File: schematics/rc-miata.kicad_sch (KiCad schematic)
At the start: 4 parts, among them M1 BLDC_MOTOR, U1 ESP32-C3-DevKitM-1, U3 ESC

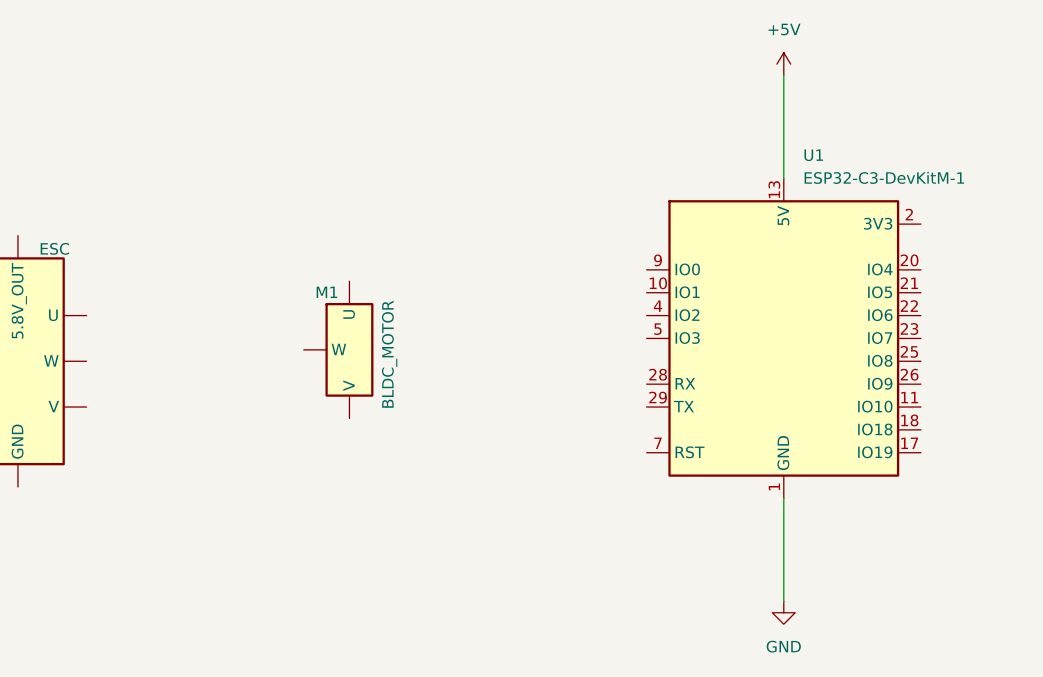
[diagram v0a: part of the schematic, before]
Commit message: Created UBEC symbol. Added UBEC to schematic unwired
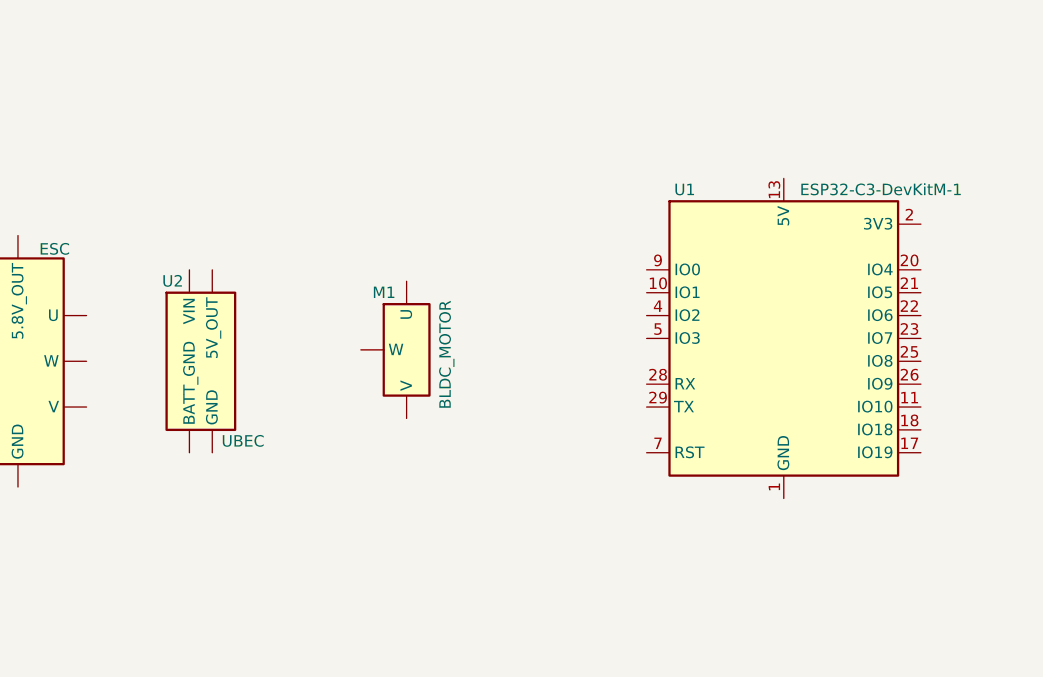
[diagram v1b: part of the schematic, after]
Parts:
- added U2: UBEC, symbol RC Components:UBEC
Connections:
- net +5V: no longer names the net of U1.13 (5V), U1.14 (5V)
- net GND: no longer names the net of U1.1 (GND), U1.12 (GND), U1.15 (GND), U1.16 (GND), U1.19 (GND), U1.24 (GND), U1.27 (GND), U1.30 (GND), U1.6 (GND), U1.8 (GND)
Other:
- moved on the sheet: M1
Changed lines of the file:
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@@
 		(company "TOFFOR AUTOS")
-	)
-	(wire
-		(pts
-			(xy 165.1 66.04) (xy 165.1 77.47)
-		)
-		(stroke
-			(width 0)
-			(type default)
-		)
-	)
-	(wire
-		(pts
-			(xy 165.1 124.46) (xy 165.1 113.03)
-		)
-		(stroke
-			(width 0)
-			(type default)
-		)
 	)
 	(symbol
@@
 		(in_pos_files yes)
 		(dnp no)
-		(fields_autoplaced yes)
 		(property "Reference" "U1"
-			(at 167.2433 74.93 0)
+			(at 152.908 78.74 0)
 			(show_name no)
 			(do_not_autoplace no)
@@
 		)
 		(property "Value" "ESP32-C3-DevKitM-1"
-			(at 167.2433 77.47 0)
+			(at 166.878 78.74 0)
 			(show_name no)
 			(do_not_autoplace no)
@@
 	(symbol
 		(lib_id "RC Components:BLDC_MOTOR")
-		(at 114.3 91.44 0)
+		(at 120.65 91.44 0)
 		(unit 1)
 		(body_style 1)
@@
 		(dnp no)
 		(property "Reference" "M1"
-			(at 113.03 90.17 0)
+			(at 119.38 90.17 0)
 			(show_name no)
 			(do_not_autoplace no)
@@
 		)
 		(property "Value" "BLDC_MOTOR"
-			(at 121.158 103.124 90)
+			(at 127.508 103.124 90)
 			(show_name no)
 			(do_not_autoplace no)
@@
 		)
 		(property "Footprint" ""
-			(at 114.3 91.44 0)
+			(at 120.65 91.44 0)
 			(hide yes)
 			(show_name no)
@@
 		)
 		(property "Datasheet" ""
-			(at 114.3 91.44 0)
+			(at 120.65 91.44 0)
 			(hide yes)
 			(show_name no)
@@
 		)
 		(property "Description" "Brushless DC motor, 3100Kv, Made for 1/10 RC Cars"
-			(at 152.4 98.552 0)
+			(at 158.75 98.552 0)
 			(hide yes)
 			(show_name no)
@@
 	)
 	(symbol
-		(lib_id "power:GND")
-		(at 165.1 124.46 0)
+		(lib_id "RC Components:UBEC")
+		(at 96.52 90.17 0)
 		(unit 1)
 		(body_style 1)
 		(exclude_from_sim no)
 		(in_bom yes)
-		(on_board yes)
+		(on_board no)
 		(in_pos_files yes)
 		(dnp no)
-		(fields_autoplaced yes)
-		(property "Reference" "#PWR02"
-			(at 165.1 130.81 0)
-			(hide yes)
-			(show_name no)
-			(do_not_autoplace no)
-			(effects
-				(font
-					(size 1.27 1.27)
-				)
-			)
-		)
-		(property "Value" "GND"
-			(at 165.1 129.54 0)
-			(show_name no)
-			(do_not_autoplace no)
-			(effects
-				(font
-					(size 1.27 1.27)
-				)
+		(property "Reference" "U2"
+			(at 96.012 88.9 0)
+			(show_name no)
+			(do_not_autoplace no)
+			(effects
+				(font
+					(size 1.27 1.27)
+				)
+				(justify left)
+			)
+		)
+		(property "Value" "UBEC"
+			(at 102.616 106.68 0)
+			(show_name no)
+			(do_not_autoplace no)
+			(effects
+				(font
+					(size 1.27 1.27)
+				)
+				(justify left)
 			)
 		)
 		(property "Footprint" ""
-			(at 165.1 124.46 0)
+			(at 96.52 90.17 0)
 			(hide yes)
 			(show_name no)
@@
 		)
 		(property "Datasheet" ""
-			(at 165.1 124.46 0)
-			(hide yes)
-			(show_name no)
-			(do_not_autoplace no)
-			(effects
-				(font
-					(size 1.27 1.27)
-				)
-			)
-		)
-		(property "Description" "Power symbol creates a global label with name \"GND\" , ground"
-			(at 165.1 124.46 0)
+			(at 96.52 90.17 0)
+			(hide yes)
+			(show_name no)
+			(do_not_autoplace no)
+			(effects
+				(font
+					(size 1.27 1.27)
+				)
+			)
+		)
+		(property "Description" "5.5V-2V IN, 5V OUT, UBEC Voltage Regulator"
+			(at 128.778 101.854 0)
 			(hide yes)
 			(show_name no)
@@
 		)
 		(pin "1"
+		)
+		(pin "2"
+		)
+		(pin "4"
+		)
+		(pin "3"
 		)
 		(instances
 			(project "rc-miata"
 				(path "/59cbdaad-7c89-4958-b9bb-08b035442600"
-					(reference "#PWR02")
+					(reference "U2")
 					(unit 1)
 				)
-			)
-		)
-	)
-	(symbol
-		(lib_id "power:+5V")
-		(at 165.1 66.04 0)
-		(unit 1)
-		(body_style 1)
-		(exclude_from_sim no)
-		(in_bom yes)
-		(on_board yes)
-		(in_pos_files yes)
-		(dnp no)
-		(fields_autoplaced yes)
-		(property "Reference" "#PWR04"
-			(at 165.1 69.85 0)
-			(hide yes)
-			(show_name no)
-			(do_not_autoplace no)
-			(effects
-				(font
-					(size 1.27 1.27)
-				)
-			)
-		)
-		(property "Value" "+5V"
-			(at 165.1 60.96 0)
-			(show_name no)
-			(do_not_autoplace no)
-			(effects
-				(font
-					(size 1.27 1.27)
-				)
-			)
-		)
-		(property "Footprint" ""
-			(at 165.1 66.04 0)
-			(hide yes)
-			(show_name no)
-			(do_not_autoplace no)
-			(effects
-				(font
-					(size 1.27 1.27)
-				)
-			)
-		)
-		(property "Datasheet" ""
-			(at 165.1 66.04 0)
-			(hide yes)
-			(show_name no)
-			(do_not_autoplace no)
-			(effects
-				(font
-					(size 1.27 1.27)
-				)
-			)
-		)
-		(property "Description" "Power symbol creates a global label with name \"+5V\""
-			(at 165.1 66.04 0)
-			(hide yes)
-			(show_name no)
-			(do_not_autoplace no)
-			(effects
-				(font
-					(size 1.27 1.27)
-				)
-			)
-		)
-		(pin "1"
-		)
-		(instances
-			(project "rc-miata"
-				(path "/59cbdaad-7c89-4958-b9bb-08b035442600"
-					(reference "#PWR04")
-					(unit 1)
-				)

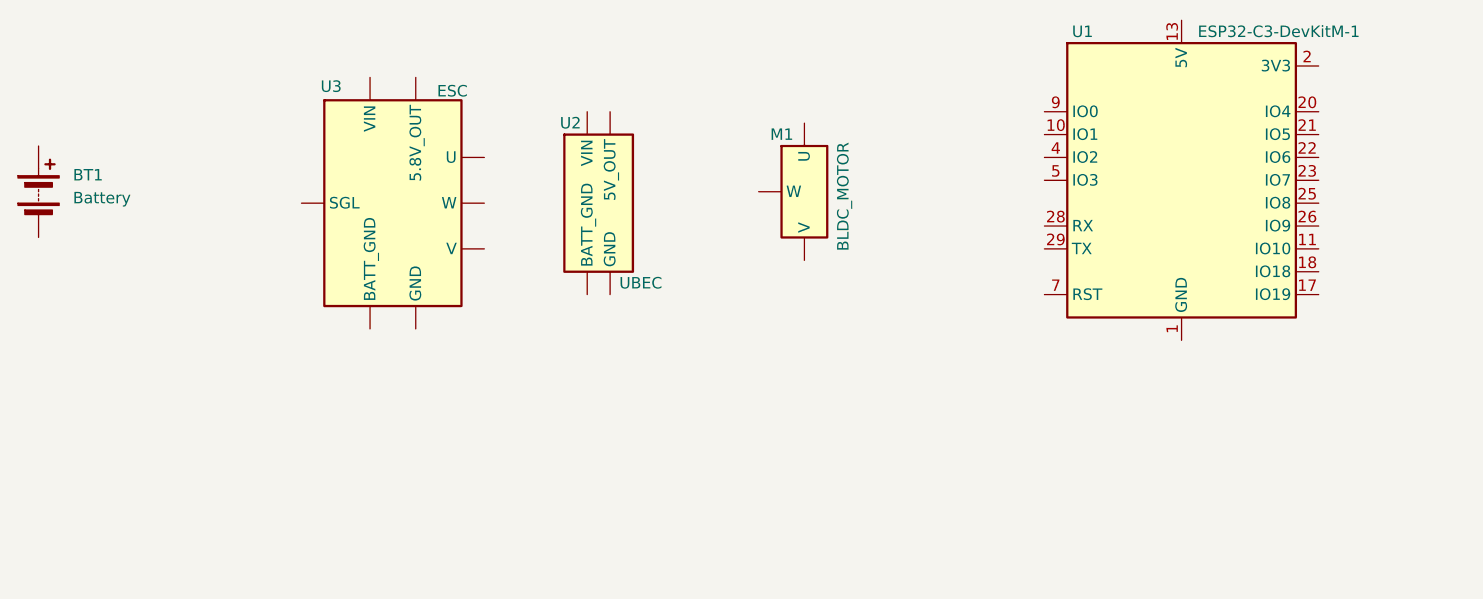
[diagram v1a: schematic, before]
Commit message: Started wiring battery circuit
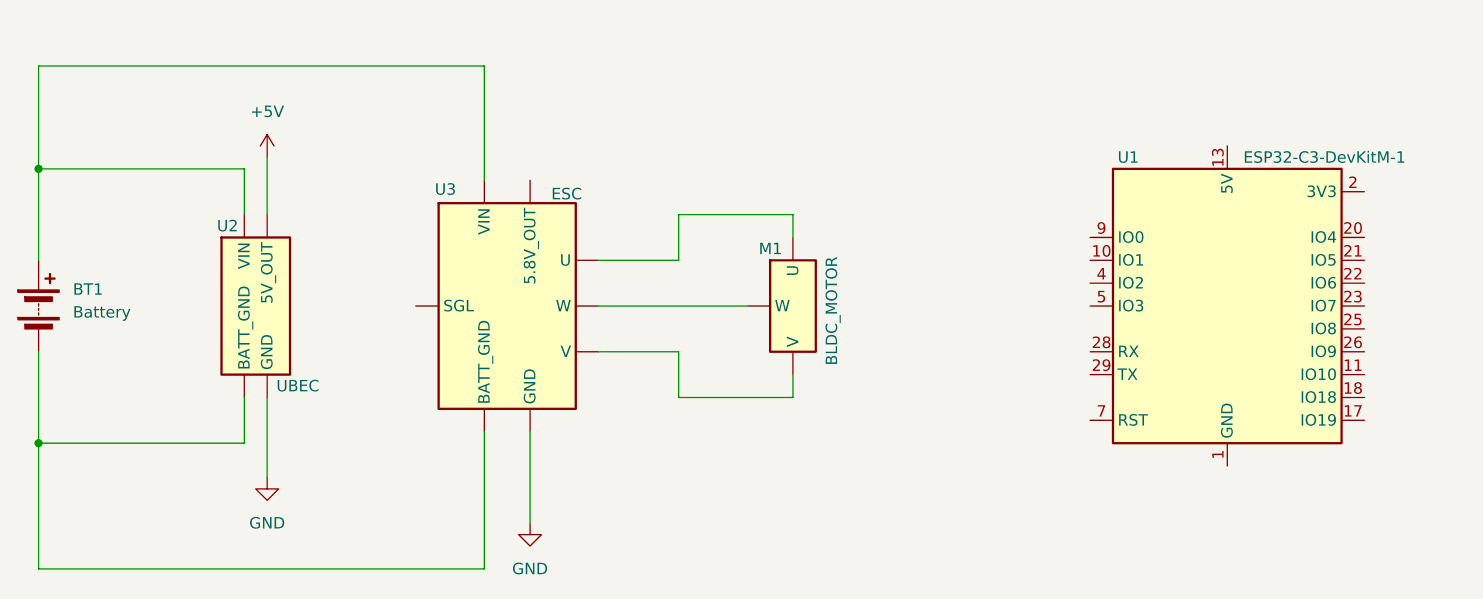
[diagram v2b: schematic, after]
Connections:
- net at M1.1 (U): now also U3.6 (U)
- net at M1.2 (V): now also U3.7 (V)
- net at M1.3 (W): now also U3.8 (W)
- net at BT1.1 (+): now also U2.1 (VIN), U3.1 (VIN)
- net at BT1.2 (-): now also U2.2 (BATT_GND), U3.2 (BATT_GND)
- net +5V: now reaches U2.3 (5V_OUT)
- net GND: now reaches U2.4 (GND)
- net GND: now also U3.4 (GND)
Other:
- moved on the sheet: BT1, M1, U1, U2, U3

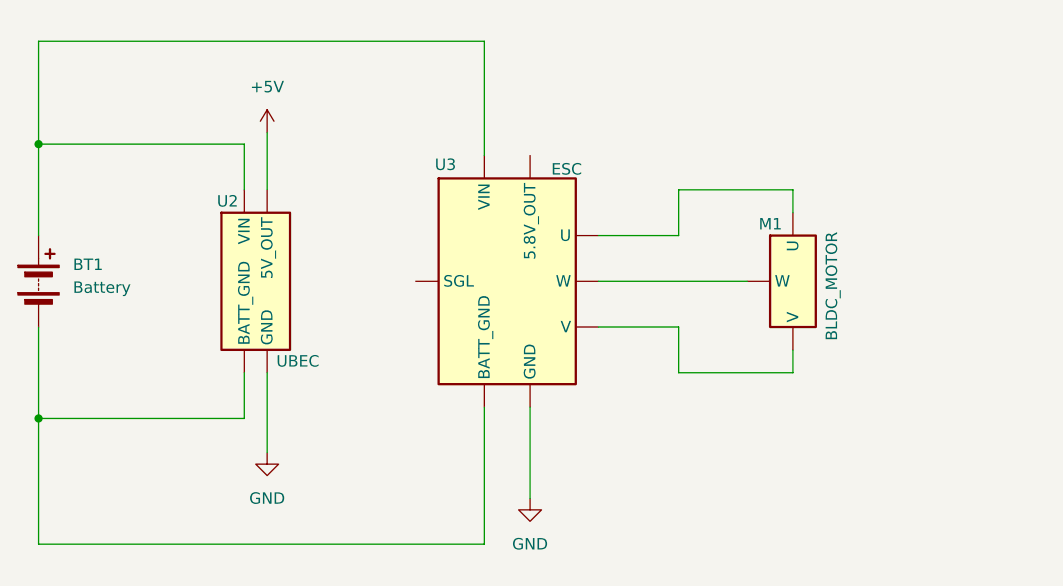
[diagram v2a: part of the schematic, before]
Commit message: Fixed Rev. Continued wiring. Chnaged 5.8V to 6V
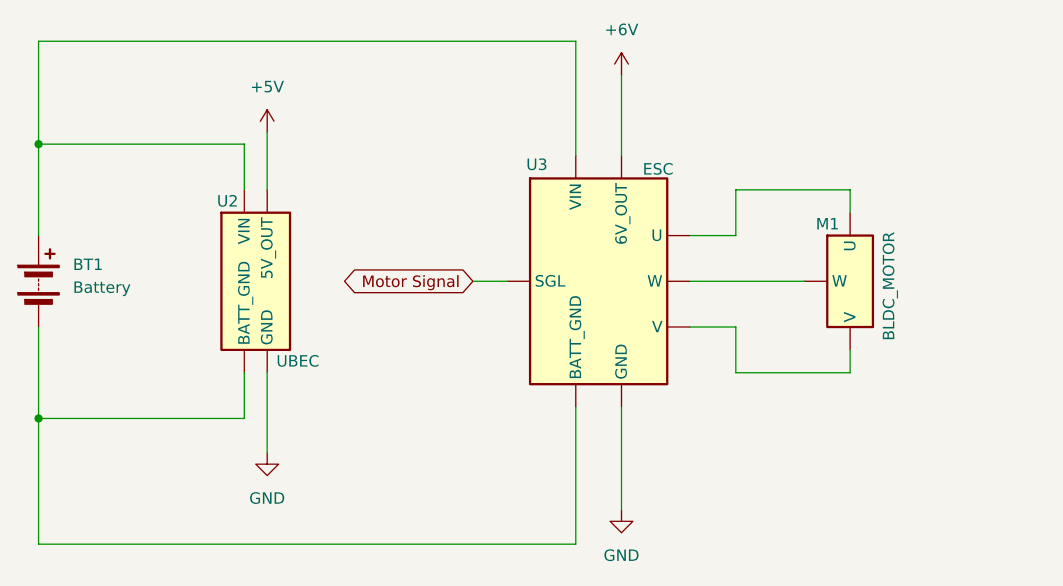
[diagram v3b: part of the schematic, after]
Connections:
- net +6V: now reaches U3.3 (6V_OUT)
- net Motor Signal: now reaches U3.5 (SGL)
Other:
- title: RC MIATA -> RC Miata
- moved on the sheet: M1, U3
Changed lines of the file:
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@@
 	(paper "A4")
 	(title_block
-		(title "RC MIATA")
-		(rev "1")
+		(title "RC Miata")
+		(rev "A")
 		(company "TOFFOR AUTOS")
 	)
@@
 	(wire
 		(pts
-			(xy 121.92 119.38) (xy 121.92 116.84)
-		)
-		(stroke
-			(width 0)
-			(type default)
-		)
-	)
-	(wire
-		(pts
-			(xy 100.33 104.14) (xy 109.22 104.14)
+			(xy 128.27 119.38) (xy 128.27 116.84)
+		)
+		(stroke
+			(width 0)
+			(type default)
+		)
+	)
+	(wire
+		(pts
+			(xy 110.49 104.14) (xy 115.57 104.14)
 		)
 		(stroke
@@
 	(wire
 		(pts
-			(xy 38.1 82.55) (xy 87.63 82.55)
+			(xy 38.1 82.55) (xy 97.79 82.55)
 		)
 		(stroke
@@
 	(wire
 		(pts
-			(xy 109.22 119.38) (xy 121.92 119.38)
-		)
-		(stroke
-			(width 0)
-			(type default)
-		)
-	)
-	(wire
-		(pts
-			(xy 109.22 104.14) (xy 109.22 99.06)
-		)
-		(stroke
-			(width 0)
-			(type default)
-		)
-	)
-	(wire
-		(pts
-			(xy 92.71 123.19) (xy 92.71 133.35)
-		)
-		(stroke
-			(width 0)
-			(type default)
-		)
-	)
-	(wire
-		(pts
-			(xy 100.33 109.22) (xy 116.84 109.22)
+			(xy 115.57 119.38) (xy 128.27 119.38)
+		)
+		(stroke
+			(width 0)
+			(type default)
+		)
+	)
+	(wire
+		(pts
+			(xy 115.57 104.14) (xy 115.57 99.06)
+		)
+		(stroke
+			(width 0)
+			(type default)
+		)
+	)
+	(wire
+		(pts
+			(xy 102.87 123.19) (xy 102.87 134.62)
+		)
+		(stroke
+			(width 0)
+			(type default)
+		)
+	)
+	(wire
+		(pts
+			(xy 110.49 109.22) (xy 123.19 109.22)
 		)
 		(stroke
@@
 	(wire
 		(pts
-			(xy 121.92 99.06) (xy 121.92 101.6)
-		)
-		(stroke
-			(width 0)
-			(type default)
-		)
-	)
-	(wire
-		(pts
-			(xy 87.63 123.19) (xy 87.63 138.43)
-		)
-		(stroke
-			(width 0)
-			(type default)
-		)
-	)
-	(wire
-		(pts
-			(xy 87.63 138.43) (xy 38.1 138.43)
+			(xy 90.17 109.22) (xy 86.36 109.22)
+		)
+		(stroke
+			(width 0)
+			(type default)
+		)
+	)
+	(wire
+		(pts
+			(xy 128.27 99.06) (xy 128.27 101.6)
+		)
+		(stroke
+			(width 0)
+			(type default)
+		)
+	)
+	(wire
+		(pts
+			(xy 102.87 95.25) (xy 102.87 86.36)
+		)
+		(stroke
+			(width 0)
+			(type default)
+		)
+	)
+	(wire
+		(pts
+			(xy 97.79 123.19) (xy 97.79 138.43)
+		)
+		(stroke
+			(width 0)
+			(type default)
+		)
+	)
+	(wire
+		(pts
+			(xy 97.79 138.43) (xy 38.1 138.43)
 		)
 		(stroke
@@
 	(wire
 		(pts
-			(xy 100.33 114.3) (xy 109.22 114.3)
+			(xy 110.49 114.3) (xy 115.57 114.3)
 		)
 		(stroke
@@
 	(wire
 		(pts
-			(xy 109.22 99.06) (xy 121.92 99.06)
+			(xy 115.57 99.06) (xy 128.27 99.06)
 		)
 		(stroke
@@
 	(wire
 		(pts
-			(xy 87.63 82.55) (xy 87.63 95.25)
-		)
-		(stroke
-			(width 0)
-			(type default)
-		)
-	)
-	(wire
-		(pts
-			(xy 109.22 114.3) (xy 109.22 119.38)
-		)
-		(stroke
-			(width 0)
-			(type default)
+			(xy 97.79 82.55) (xy 97.79 95.25)
+		)
+		(stroke
+			(width 0)
+			(type default)
+		)
+	)
+	(wire
+		(pts
+			(xy 115.57 114.3) (xy 115.57 119.38)
+		)
+		(stroke
+			(width 0)
+			(type default)
+		)
+	)
+	(global_label "Motor Signal"
+		(shape bidirectional)
+		(at 86.36 109.22 180)
+		(fields_autoplaced yes)
+		(effects
+			(font
+				(size 1.27 1.27)
+			)
+			(justify right)
+		)
+		(property "Intersheetrefs" "${INTERSHEET_REFS}"
+			(at 70.1081 109.22 0)
+			(hide yes)
+			(show_name no)
+			(do_not_autoplace no)
+			(effects
+				(font
+					(size 1.27 1.27)
+				)
+				(justify right)
+			)
 		)
 	)
@@
 	(symbol
 		(lib_id "RC Components:BLDC_MOTOR")
-		(at 119.38 104.14 0)
+		(at 125.73 104.14 0)
 		(unit 1)
 		(body_style 1)
@@
 		(dnp no)
 		(property "Reference" "M1"
-			(at 118.11 102.87 0)
+			(at 124.46 102.87 0)
 			(show_name no)
 			(do_not_autoplace no)
@@
 		)
 		(property "Value" "BLDC_MOTOR"
-			(at 126.238 115.824 90)
+			(at 132.588 115.824 90)
 			(show_name no)
 			(do_not_autoplace no)
@@
 		)
 		(property "Footprint" ""
-			(at 119.38 104.14 0)
+			(at 125.73 104.14 0)
 			(hide yes)
 			(show_name no)
@@
 		)
 		(property "Datasheet" ""
-			(at 119.38 104.14 0)
+			(at 125.73 104.14 0)
 			(hide yes)
 			(show_name no)
@@
 		)
 		(property "Description" "Brushless DC motor, 3100Kv, Made for 1/10 RC Cars"
-			(at 157.48 111.252 0)
+			(at 163.83 111.252 0)
 			(hide yes)
 			(show_name no)
@@
 	)
 	(symbol
+		(lib_id "power:+6V")
+		(at 102.87 86.36 0)
+		(unit 1)
+		(body_style 1)
+		(exclude_from_sim no)
+		(in_bom yes)
+		(on_board yes)
+		(in_pos_files yes)
+		(dnp no)
+		(fields_autoplaced yes)
+		(property "Reference" "#PWR04"
+			(at 102.87 90.17 0)
+			(hide yes)
+			(show_name no)
+			(do_not_autoplace no)
+			(effects
+				(font
+					(size 1.27 1.27)
+				)
+			)
+		)
+		(property "Value" "+6V"
+			(at 102.87 81.28 0)
+			(show_name no)
+			(do_not_autoplace no)
+			(effects
+				(font
+					(size 1.27 1.27)
+				)
+			)
+		)
+		(property "Footprint" ""
+			(at 102.87 86.36 0)
+			(hide yes)
+			(show_name no)
+			(do_not_autoplace no)
+			(effects
+				(font
+					(size 1.27 1.27)
+				)
+			)
+		)
+		(property "Datasheet" ""
+			(at 102.87 86.36 0)
+			(hide yes)
+			(show_name no)
+			(do_not_autoplace no)
+			(effects
+				(font
+					(size 1.27 1.27)
+				)
+			)
+		)
+		(property "Description" "Power symbol creates a global label with name \"+6V\""
+			(at 102.87 86.36 0)
+			(hide yes)
+			(show_name no)
+			(do_not_autoplace no)
+			(effects
+				(font
+					(size 1.27 1.27)
+				)
+			)
+		)
+		(pin "1"
+		)
+		(instances
+			(project "rc-miata"
+				(path "/59cbdaad-7c89-4958-b9bb-08b035442600"
+					(reference "#PWR04")
+					(unit 1)
+				)
+			)
+		)
+	)
+	(symbol
 		(lib_id "RC Components:60A_BRUSHLESS_ESC")
-		(at 82.55 97.79 0)
+		(at 92.71 97.79 0)
 		(unit 1)
 		(body_style 1)
@@
 		(dnp no)
 		(property "Reference" "U3"
-			(at 83.312 96.266 0)
+			(at 93.472 96.266 0)
 			(show_name no)
 			(do_not_autoplace no)
@@
 		)
 		(property "Value" "ESC"
-			(at 96.774 96.774 0)
+			(at 106.934 96.774 0)
 			(show_name no)
 			(do_not_autoplace no)
@@
 		)
 		(property "Footprint" ""
-			(at 82.55 97.79 0)
+			(at 92.71 97.79 0)
 			(hide yes)
 			(show_name no)
@@
 		)
 		(property "Datasheet" ""
-			(at 82.55 97.79 0)
+			(at 92.71 97.79 0)
 			(hide yes)
 			(show_name no)
@@
 		)
 		(property "Description" "60A, Brushless Electronic Speed Controller, Made for 1/10 RC Car"
-			(at 135.128 116.84 0)
+			(at 145.288 116.84 0)
 			(hide yes)
 			(show_name no)
@@
 	(symbol
 		(lib_id "power:GND")
-		(at 92.71 133.35 0)
+		(at 102.87 134.62 0)
 		(unit 1)
 		(body_style 1)
@@
 		(fields_autoplaced yes)
 		(property "Reference" "#PWR03"
-			(at 92.71 139.7 0)
+			(at 102.87 140.97 0)
 			(hide yes)
 			(show_name no)
@@
 		)
 		(property "Value" "GND"
-			(at 92.71 138.43 0)
+			(at 102.87 139.7 0)
 			(show_name no)
 			(do_not_autoplace no)
@@
 		)
 		(property "Footprint" ""
-			(at 92.71 133.35 0)
+			(at 102.87 134.62 0)
 			(hide yes)
 			(show_name no)
@@
 		)
 		(property "Datasheet" ""
-			(at 92.71 133.35 0)
+			(at 102.87 134.62 0)
 			(hide yes)
 			(show_name no)
@@
 		)
 		(property "Description" "Power symbol creates a global label with name \"GND\" , ground"
-			(at 92.71 133.35 0)
-			(hide yes)
-			(show_name no)
+			(at 102.87 134.62 0)
+			(hide yes)
+			(show_name no)
